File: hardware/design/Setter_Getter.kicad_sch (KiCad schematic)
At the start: 12 parts, among them Q4801 2N7000, U4801 LM393, U4802 ADG417, U4803 ADG417

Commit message: Editorial change
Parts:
- renumbered R4804 to R4801, R4806 to R4802, R4801 to R4803, R4802 to R4804, R4803 to R4806, U4803 to U4802, U4802 to U4803

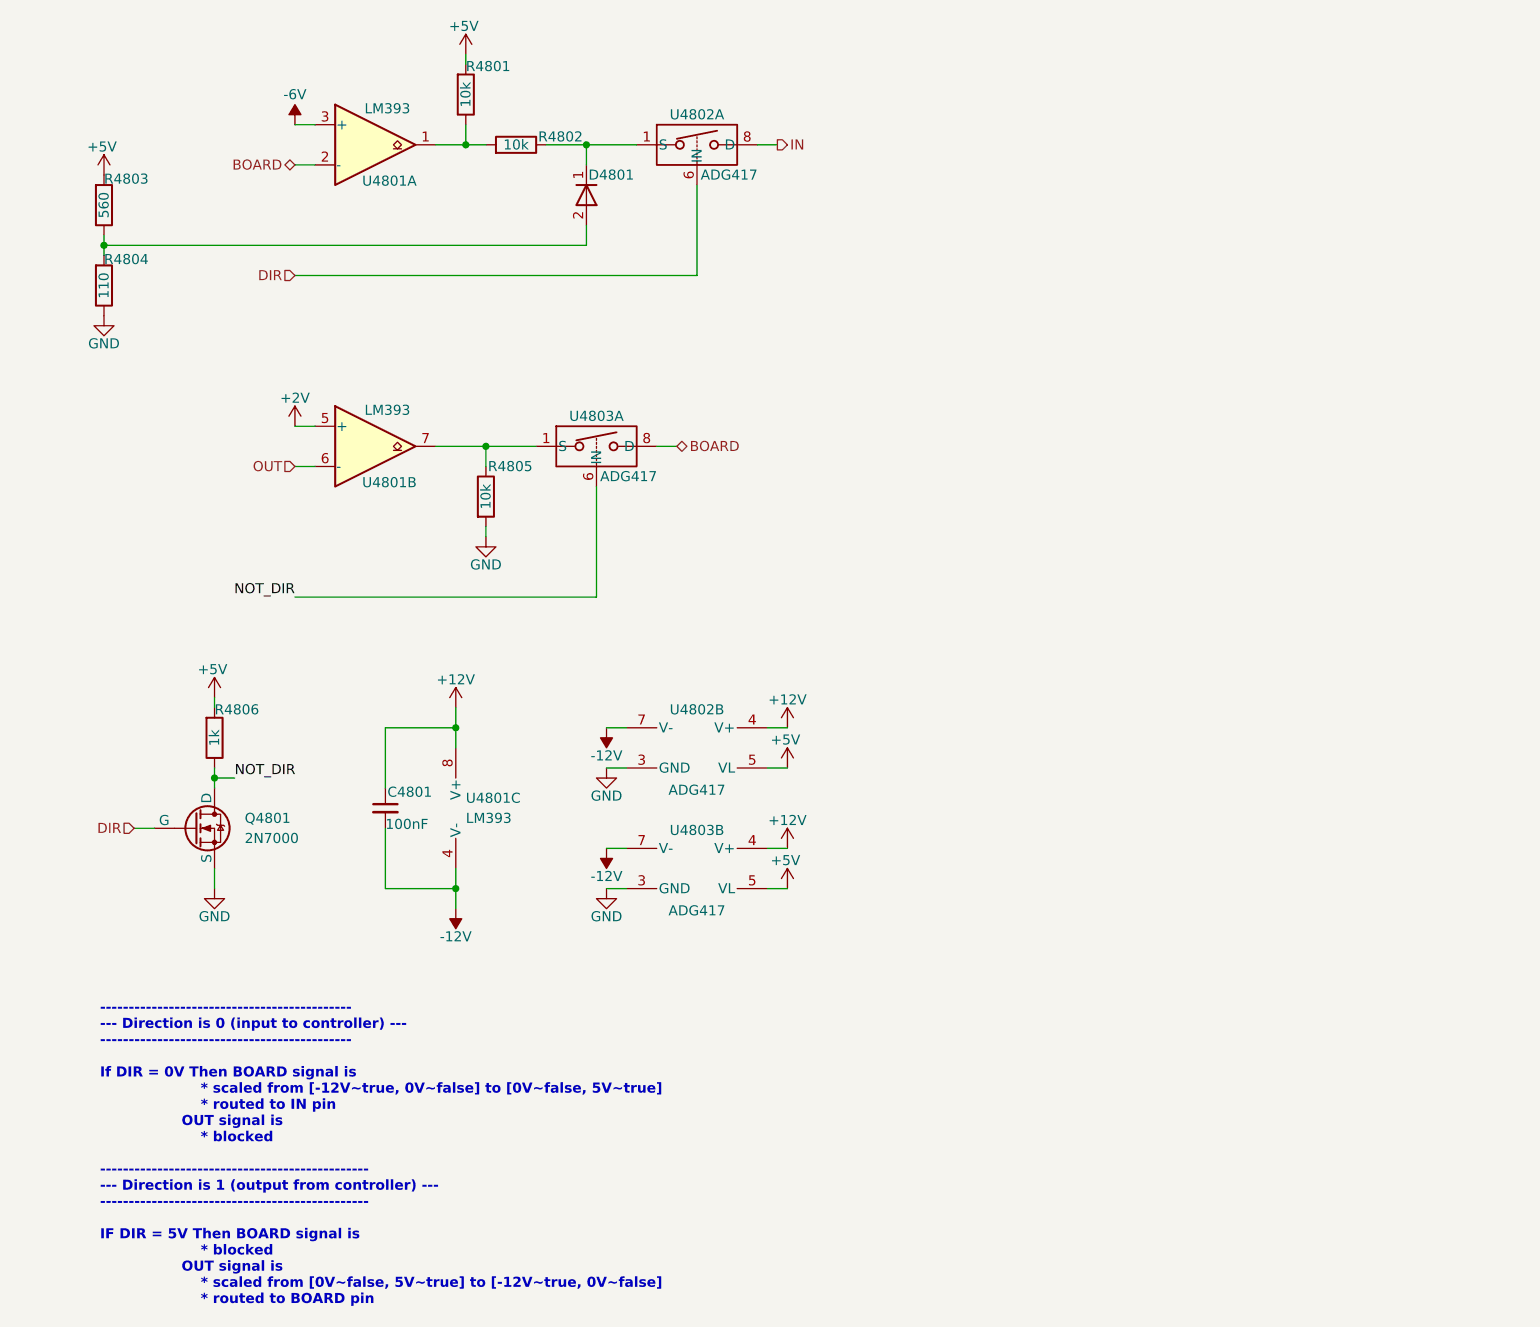
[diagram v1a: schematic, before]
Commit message: Replaced solid state relay with electromechanical relay
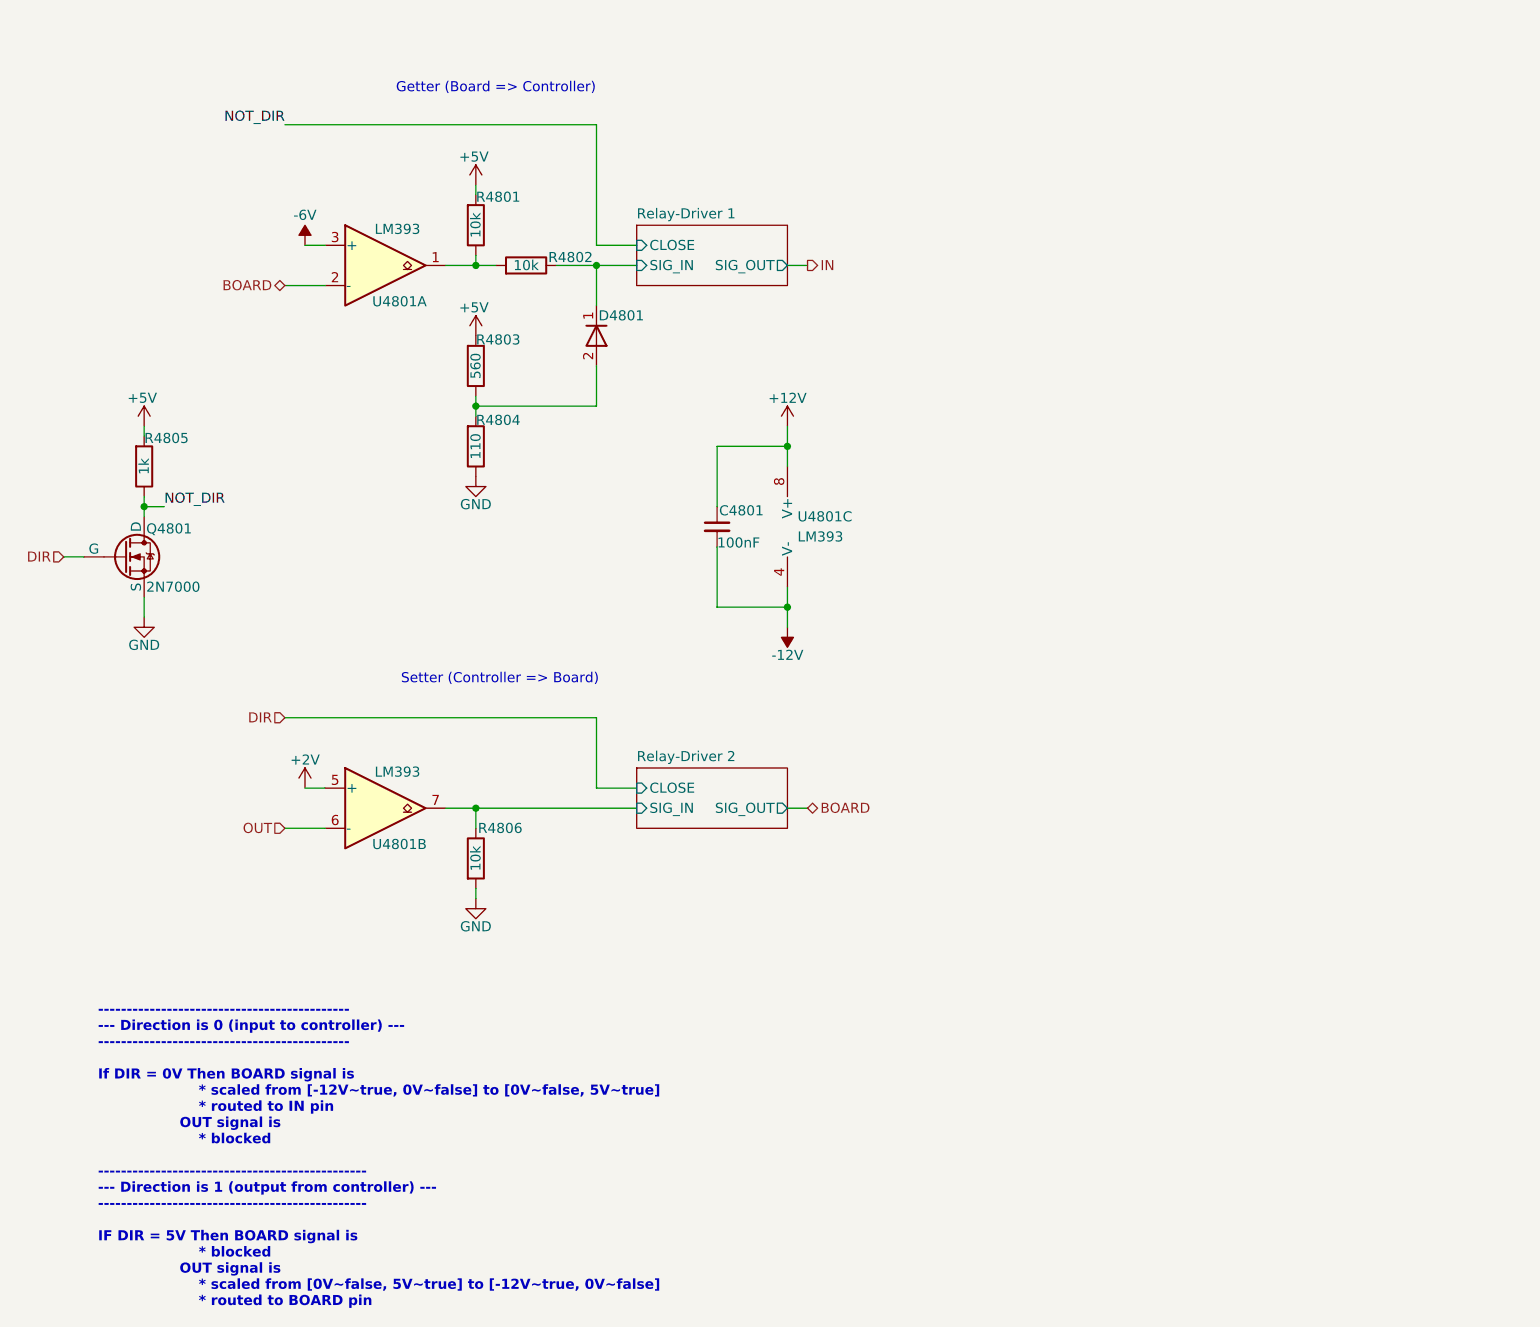
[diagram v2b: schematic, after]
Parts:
- removed U4802, U4803: ADG417, Package_DIP:DIP-8_W7.62mm, symbol ADG417:ADG417
- Q4801: footprint (none) -> Package_TO_SOT_THT:TO-92_Inline
- renumbered R4806 to R4805, R4805 to R4806
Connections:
- net Relay-Driver 2/SIG_IN: now reaches R4806.1, U4801.7
- net Relay-Driver 1/SIG_IN: now reaches D4801.1 (K), R4802.1
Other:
- added sheet Relay-Driver 1 (Relay-Driver.kicad_sch)
- added sheet Relay-Driver 2 (Relay-Driver.kicad_sch)
- note added: "Getter (Board => Controller)"
- note added: "Setter (Controller => Board)"
- moved on the sheet: C4801, D4801, Q4801, R4801, R4802, R4803, R4804, R4805, R4806, U4801A, U4801B, U4801C

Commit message: Simulating alternative power supply
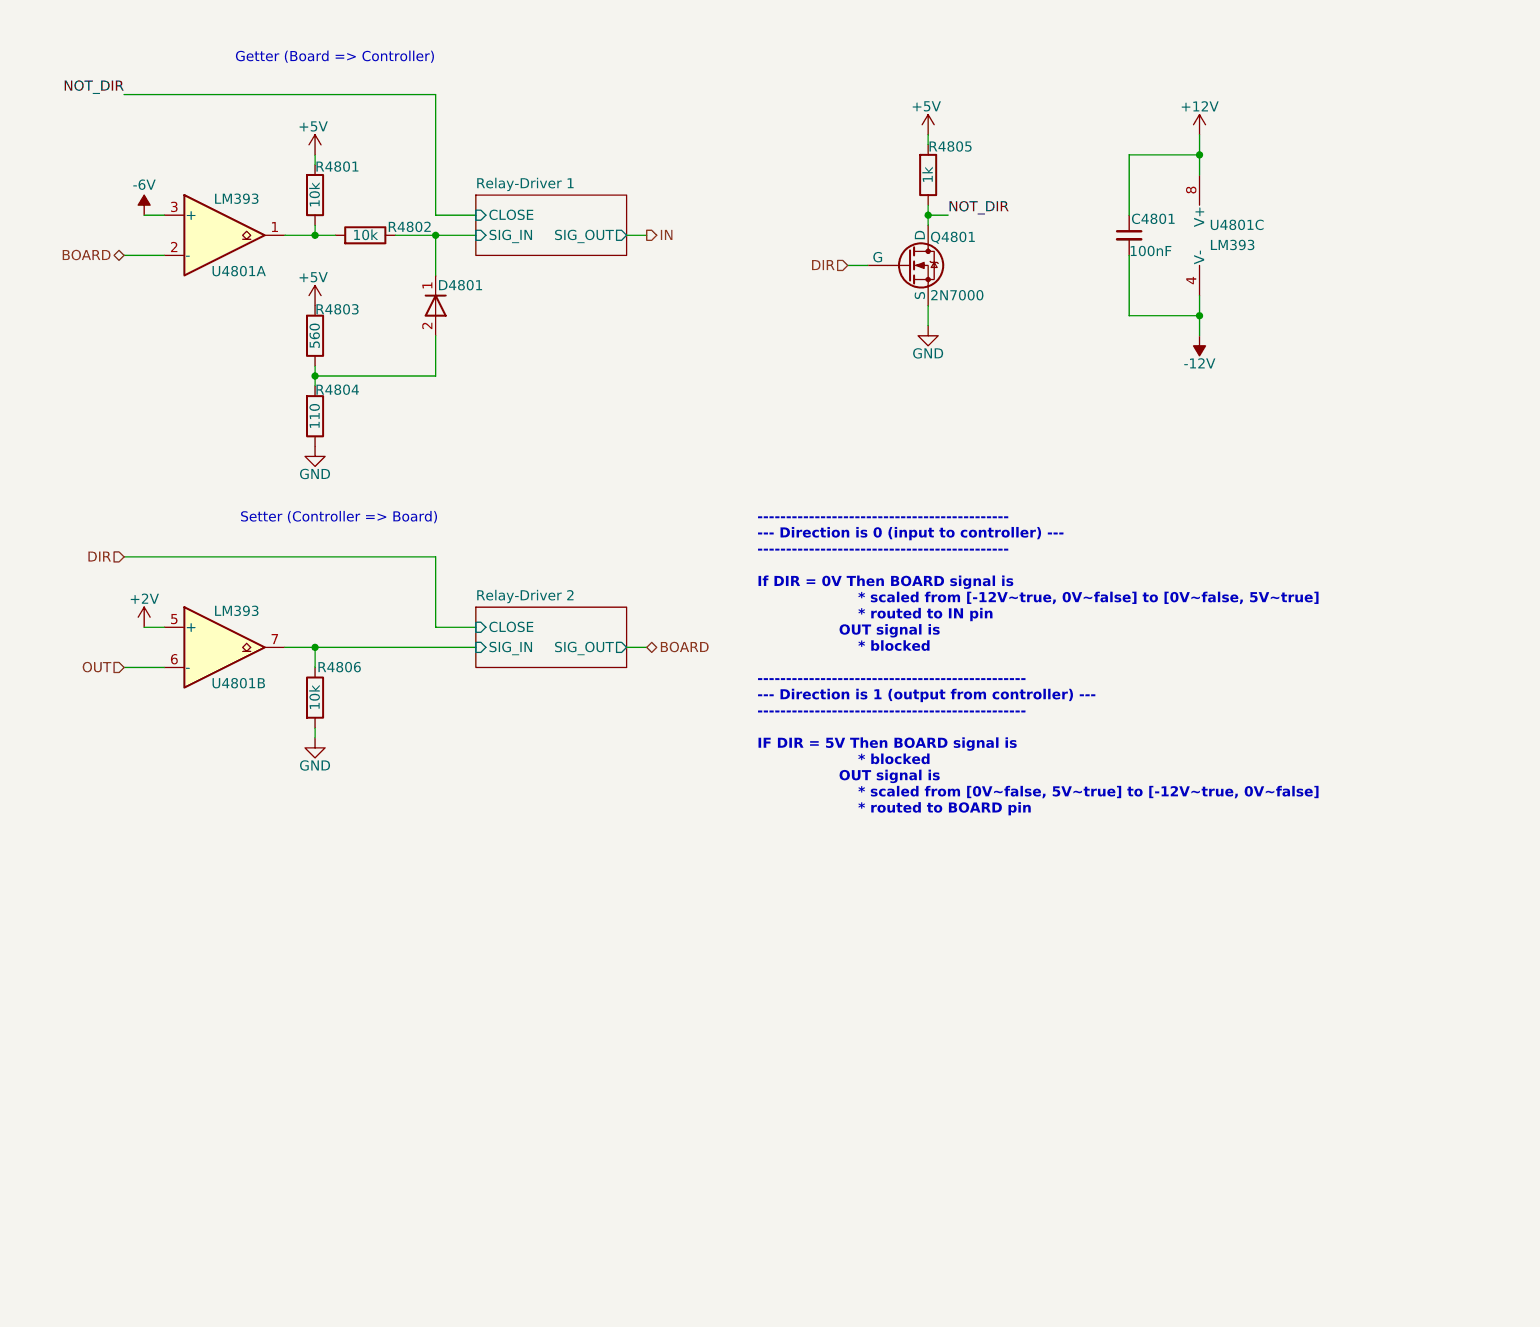
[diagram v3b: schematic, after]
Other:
- moved on the sheet: C4801, D4801, Q4801, R4801, R4802, R4803, R4804, R4805, R4806, U4801A, U4801B, U4801C

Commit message: Finished proof of concept Relay_Driver
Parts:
- renumbered R4805 to R4801, R4801 to R4802, R4802 to R4803, R4803 to R4804, R4804 to R4805
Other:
- sheet Relay-Driver 1 renamed Relay_Driver 1
- sheet Relay-Driver 2 renamed Relay_Driver 2
- sheet Relay_Driver 1: file Relay-Driver.kicad_sch -> Relay_Driver.kicad_sch
- sheet Relay_Driver 2: file Relay-Driver.kicad_sch -> Relay_Driver.kicad_sch
